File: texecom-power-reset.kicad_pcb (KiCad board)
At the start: 2 copper layers, 0 parts

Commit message: Add PCB rev A, milling footprints, fab files and project summary
- PCB rev A (92 x 70 mm, 2-layer, CNC-milled): placed and routed with the
  KiCad routing tools at 0.8 mm clearance, 15 wire-link vias, GND pours;
  DRC 0 violations / 0 unconnected, connectivity verified against schematic
- Milling footprint variants (oval enlarged pads; per-pad top keepouts on
  parts whose body covers the top pads) and custom .kicad_dru rules
- Schematic footprints assigned to the milling variants
- Gerbers (F.Cu, B.Cu, Edge.Cuts) and Excellon drill in fab/
- Copper renders and assembly drawing in docs/
- project-summary.html: one-page visual summary, linked from the README
- README: PCB section, drill table, assembly notes, decisions

Co-Authored-By: Claude Opus 5.5 <noreply@anthropic.com>
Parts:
- added C1: 100uF, texecom-power-reset:CP_Radial_D6.3mm_P2.50mm_Mill, F.Cu at (175.0, 154.0)
- added C2: 100nF, texecom-power-reset:C_Disc_D5.0mm_W2.5mm_P5.00mm_Mill, F.Cu at (166.0, 154.0)
- added C3: 10uF, texecom-power-reset:CP_Radial_D5.0mm_P2.50mm_Mill, F.Cu at (174.0, 146.0)
- added C4: 100nF, texecom-power-reset:C_Disc_D5.0mm_W2.5mm_P5.00mm_Mill, F.Cu at (132.5, 125.5)
- added C5: 10uF, Capacitor_SMD:C_1206_3216Metric_Pad1.33x1.80mm_HandSolder, B.Cu at (152.0, 113.0)
- added C6: 10uF, Capacitor_SMD:C_1206_3216Metric_Pad1.33x1.80mm_HandSolder, B.Cu at (128.5, 113.0)
- added C7: 100nF, texecom-power-reset:C_Disc_D5.0mm_W2.5mm_P5.00mm_Mill, F.Cu at (164.0, 116.0)
- added C8: 100nF, texecom-power-reset:C_Disc_D5.0mm_W2.5mm_P5.00mm_Mill, F.Cu at (116.0, 116.5)
- added D1: 1N5822, texecom-power-reset:D_DO-201AD_P15.24mm_Mill, F.Cu at (156.0, 148.0)
- added D2: P6KE18A, texecom-power-reset:D_DO-15_P10.16mm_Mill, F.Cu at (161.0, 161.0)
- added D3: 1N5822, texecom-power-reset:D_DO-201AD_P15.24mm_Mill, F.Cu at (184.0, 128.0)
- added D4: 1N4007, texecom-power-reset:D_DO-41_P10.16mm_Mill, F.Cu at (151.0, 150.5)
- added D5: 1N4007, texecom-power-reset:D_DO-41_P10.16mm_Mill, F.Cu at (125.0, 150.5)
- added D6: RED, texecom-power-reset:LED_D3.0mm_Mill, F.Cu at (148.0, 134.0)
- added D7: RED, texecom-power-reset:LED_D3.0mm_Mill, F.Cu at (122.0, 134.0)
- added F1: PTC 0.5A, Fuse:Fuse_1206_3216Metric_Pad1.42x1.75mm_HandSolder, B.Cu at (152.0, 162.0)
- added J1: BAT IN, texecom-power-reset:KF301-2P_P5.00mm_Mill, F.Cu at (142.0, 164.0)
- added J2: BAT OUT, texecom-power-reset:KF301-2P_P5.00mm_Mill, F.Cu at (130.0, 164.0)
- added J3: AC IN, texecom-power-reset:KF301-2P_P5.00mm_Mill, F.Cu at (116.0, 164.0)
- added J4: AC OUT, texecom-power-reset:KF301-2P_P5.00mm_Mill, F.Cu at (104.0, 164.0)
- added K1: SRD-05VDC, texecom-power-reset:Relay_SRD_Form_C_Mill, F.Cu at (146.6, 146.0)
- added K2: SRD-05VDC, texecom-power-reset:Relay_SRD_Form_C_Mill, F.Cu at (120.6, 146.0)
- added MH1: M3, MountingHole:MountingHole_3.2mm_M3, F.Cu at (104.0, 104.0)
- added MH2: M3, MountingHole:MountingHole_3.2mm_M3, F.Cu at (186.0, 166.0)
- added Q1: 2N2222A, texecom-power-reset:TO-92_Inline_Wide_Mill, F.Cu at (139.0, 134.0)
- added Q2: 2N2222A, texecom-power-reset:TO-92_Inline_Wide_Mill, F.Cu at (113.0, 134.0)
- added R1: 100k, texecom-power-reset:R_Axial_DIN0207_P10.16mm_Mill, F.Cu at (149.0, 108.0)
- added R10: 1k, Resistor_SMD:R_1206_3216Metric_Pad1.30x1.75mm_HandSolder, B.Cu at (165.0, 124.0)
- added R11: 100, Resistor_SMD:R_1206_3216Metric_Pad1.30x1.75mm_HandSolder, B.Cu at (152.0, 119.5)
- added R12: 100, Resistor_SMD:R_1206_3216Metric_Pad1.30x1.75mm_HandSolder, B.Cu at (128.5, 119.5)
- added R13: 10k, texecom-power-reset:R_Axial_DIN0207_P10.16mm_Mill, F.Cu at (131.5, 129.0)
- added R14: 10k, texecom-power-reset:R_Axial_DIN0207_P10.16mm_Mill, F.Cu at (105.5, 129.0)
- added R15: 1k, Resistor_SMD:R_1206_3216Metric_Pad1.30x1.75mm_HandSolder, B.Cu at (150.5, 129.0)
- added R16: 1k, Resistor_SMD:R_1206_3216Metric_Pad1.30x1.75mm_HandSolder, B.Cu at (124.5, 129.0)
- added R2: 100k, texecom-power-reset:R_Axial_DIN0207_P10.16mm_Mill, F.Cu at (111.0, 108.0)
- added R3: 1M, texecom-power-reset:R_Axial_DIN0207_P10.16mm_Mill, F.Cu at (156.0, 122.0)
- added R4: 1M, texecom-power-reset:R_Axial_DIN0207_P10.16mm_Mill, F.Cu at (124.5, 122.0)
- added R5: 10k, texecom-power-reset:R_Axial_DIN0207_P10.16mm_Mill, F.Cu at (149.0, 104.0)
- added R6: 10k, texecom-power-reset:R_Axial_DIN0207_P10.16mm_Mill, F.Cu at (111.0, 104.0)
- added R7: 1k, Resistor_SMD:R_1206_3216Metric_Pad1.30x1.75mm_HandSolder, B.Cu at (133.0, 132.5)
- added R8: 1k, Resistor_SMD:R_1206_3216Metric_Pad1.30x1.75mm_HandSolder, B.Cu at (107.0, 132.5)
- added R9: 1k, Resistor_SMD:R_1206_3216Metric_Pad1.30x1.75mm_HandSolder, B.Cu at (165.0, 108.0)
- added U1: Pololu S9V11E2F5, texecom-power-reset:Pololu_S9V11E2x_Mill, F.Cu at (161.0, 148.0)
- added U2: 74HCT4538, texecom-power-reset:DIP-16_W7.62mm_Socket_Mill, F.Cu at (144.0, 121.0)
- added U3: ESP32-C3 SuperMini, texecom-power-reset:ESP32-C3-SuperMini_Mill, F.Cu at (180.0, 111.0)
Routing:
- net +5V: track 0.00 -> 192.0 mm, vias 0 -> 2
- net Net-(U2B-R): track 0.00 -> 111.7 mm, vias 0 -> 2
- net Net-(U2B-Q): track 0.00 -> 64.8 mm
- net Net-(C5-Pad2): track 0.00 -> 54.3 mm, vias 0 -> 2
- net Net-(D4-A): track 0.00 -> 45.3 mm, vias 0 -> 1
- net Net-(U2A-R): track 0.00 -> 39.7 mm, vias 0 -> 1
- net Net-(D1-K): track 0.00 -> 37.0 mm
- net Net-(U2A-Clk+): track 0.00 -> 33.5 mm, vias 0 -> 1
- net GND: track 0.00 -> 33.5 mm, vias 0 -> 2
- net Net-(J1-Pin_1): track 0.00 -> 33.1 mm
- net Net-(U2B-Clk+): track 0.00 -> 32.7 mm
- net Net-(J3-Pin_1): track 0.00 -> 30.4 mm
- net Net-(U2A-Q): track 0.00 -> 29.4 mm, vias 0 -> 2
- net Net-(U3-IO3): track 0.00 -> 24.6 mm
- net +5V_MCU: track 0.00 -> 22.3 mm
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- added copper zone on B.Cu, net GND
- added copper zone on F.Cu, net GND
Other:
- board outline added: 92 x 70 mm

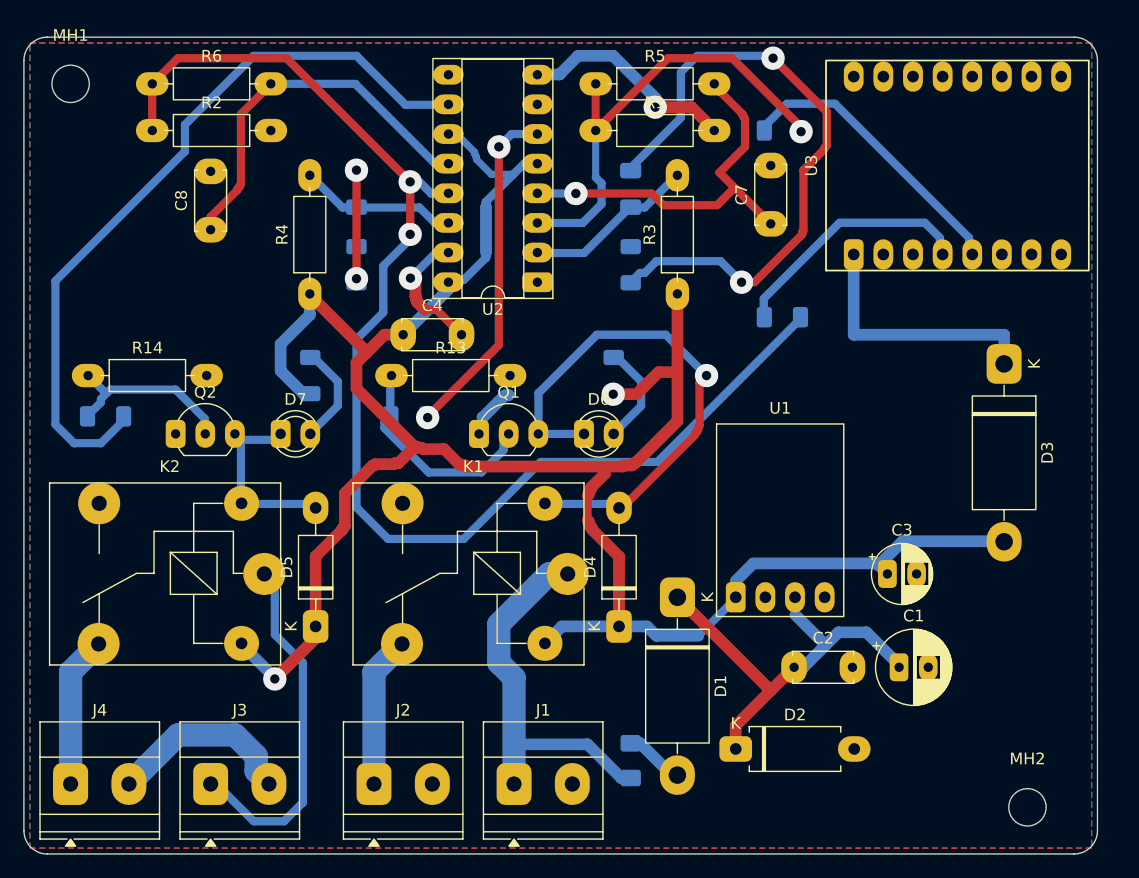
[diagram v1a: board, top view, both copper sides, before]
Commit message: Remove top GND pour and add engraved Mill_Legend layer
- GND poured on the bottom layer only; three GND pads rejoined with
  short bottom tracks and one extra via (16 vias total)
- New Mill_Legend layer (User.1): part outlines, polarity marks,
  references and BAT IN / BAT OUT / AC IN / AC OUT labels, kept 0.35mm
  clear of all top copper; exported as fab/*-Mill_Legend.gbr
- tools/make_legend.py regenerates the legend after layout changes
- Regenerated fab/ Gerbers and drill, docs/ renders
- README and project summary updated

Co-Authored-By: Claude Opus 5.5 <noreply@anthropic.com>
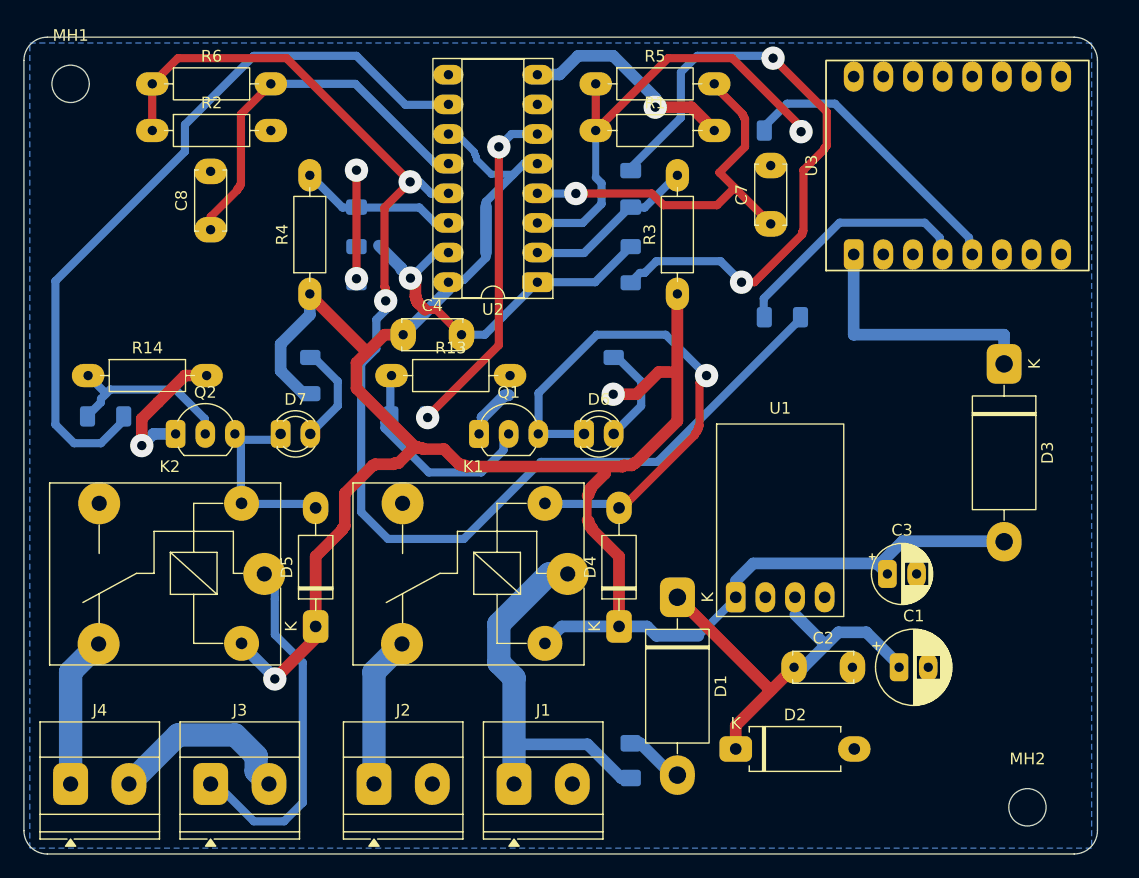
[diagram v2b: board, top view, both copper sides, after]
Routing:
- net GND: track 33.5 -> 66.8 mm, vias 2 -> 3
- removed copper zone on F.Cu, net GND
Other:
- board text added: "+"
- board text added: "-"
- board text added: "AC IN"
- board text added: "AC OUT"
- board text added: "BAT IN"
- board text added: "BAT OUT"
- board text added: "C1"
- board text added: "C2"
- board text added: "C3"
- board text added: "C4"
- board text added: "C7"
- board text added: "C8"
- board text added: "D1"
- board text added: "D2"
- board text added: "D3"
- board text added: "D4"
- board text added: "D5"
- board text added: "D6"
- board text added: "D7"
- board text added: "J1"
- board text added: "J2"
- board text added: "J3"
- board text added: "J4"
- board text added: "K1"
- board text added: "K2"
- board text added: "Q1"
- board text added: "Q2"
- board text added: "R1"
- board text added: "R13"
- board text added: "R14"
- board text added: "R2"
- board text added: "R3"
- board text added: "R4"
- board text added: "R5"
- board text added: "R6"
- board text added: "U1"
- board text added: "U2"
- board text added: "U3"

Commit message: Mark top-joint pads on the legend and add solder-top table
- Engraved ring beside each of the 20 pads that carry a top track,
  with a "o = SOLDER TOP" key; each ring is clearly nearest its pad
- README assembly step 3: table of axial/disc parts and the pads
  that must be soldered on top
- Regenerated legend Gerber, top copper SVG, assembly PDF and summary

Co-Authored-By: Claude Opus 5.5 <noreply@anthropic.com>
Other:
- board text added: "= SOLDER TOP"
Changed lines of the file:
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@@
 		(layer "User.1")
 	)
+	(gr_circle
+		(center 108.878237 105.225)
+		(end 109.378237 105.225)
+		(stroke
+			(width 0.15)
+			(type default)
+		)
+		(fill no)
+		(layer "User.1")
+	)
 	(gr_line
 		(start 109.65 145.95)
@@
 		(layer "User.1")
 	)
+	(gr_circle
+		(center 112.225 110.121762)
+		(end 112.725 110.121762)
+		(stroke
+			(width 0.15)
+			(type default)
+		)
+		(fill no)
+		(layer "User.1")
+	)
 	(gr_line
 		(start 112.55 144.15)
@@
 		(layer "User.1")
 	)
+	(gr_circle
+		(center 118.11 129)
+		(end 118.61 129)
+		(stroke
+			(width 0.15)
+			(type default)
+		)
+		(fill no)
+		(layer "User.1")
+	)
 	(gr_line
 		(start 118.114284 153.8)
@@
 		(layer "User.1")
 	)
+	(gr_circle
+		(center 118.45 116.5)
+		(end 118.95 116.5)
+		(stroke
+			(width 0.15)
+			(type default)
+		)
+		(fill no)
+		(layer "User.1")
+	)
 	(gr_line
 		(start 118.733984 105.37)
@@
 		(layer "User.1")
 	)
+	(gr_circle
+		(center 123.281762 105.225)
+		(end 123.781762 105.225)
+		(stroke
+			(width 0.15)
+			(type default)
+		)
+		(fill no)
+		(layer "User.1")
+	)
 	(gr_line
 		(start 123.36566 132.0123)
@@
 		(layer "User.1")
 	)
+	(gr_circle
+		(center 126.95 122)
+		(end 127.45 122)
+		(stroke
+			(width 0.15)
+			(type default)
+		)
+		(fill no)
+		(layer "User.1")
+	)
+	(gr_circle
+		(center 127.121762 151.725)
+		(end 127.621762 151.725)
+		(stroke
+			(width 0.15)
+			(type default)
+		)
+		(fill no)
+		(layer "User.1")
+	)
 	(gr_line
 		(start 127.38 158.68)
@@
 		(layer "User.1")
 	)
+	(gr_circle
+		(center 129.409037 124.671779)
+		(end 129.909037 124.671779)
+		(stroke
+			(width 0.15)
+			(type default)
+		)
+		(fill no)
+		(layer "User.1")
+	)
 	(gr_line
 		(start 129.699999 168.72)
@@
 		(layer "User.1")
 	)
+	(gr_circle
+		(center 138.725 123.378237)
+		(end 139.225 123.378237)
+		(stroke
+			(width 0.15)
+			(type default)
+		)
+		(fill no)
+		(layer "User.1")
+	)
 	(gr_line
 		(start 139.19 122.33)
@@
 		(layer "User.1")
 	)
+	(gr_circle
+		(center 147.775 101.878237)
+		(end 148.275 101.878237)
+		(stroke
+			(width 0.15)
+			(type default)
+		)
+		(fill no)
+		(layer "User.1")
+	)
 	(gr_line
 		(start 148 144.269707)
@@
 		(layer "User.1")
 	)
+	(gr_circle
+		(center 148.878237 151.725)
+		(end 149.378237 151.725)
+		(stroke
+			(width 0.15)
+			(type default)
+		)
+		(fill no)
+		(layer "User.1")
+	)
 	(gr_line
 		(start 148.937911 132.541165)
@@
 		(layer "User.1")
 	)
+	(gr_circle
+		(center 150.225 110.121762)
+		(end 150.725 110.121762)
+		(stroke
+			(width 0.15)
+			(type default)
+		)
+		(fill no)
+		(layer "User.1")
+	)
 	(gr_line
 		(start 150.263296 132.275626)
@@
 		(layer "User.1")
 	)
+	(gr_circle
+		(center 153.45 140.34)
+		(end 153.95 140.34)
+		(stroke
+			(width 0.15)
+			(type default)
+		)
+		(fill no)
+		(layer "User.1")
+	)
 	(gr_line
 		(start 154.63 115.155846)
@@
 		(layer "User.1")
 	)
+	(gr_circle
+		(center 156 145.25)
+		(end 156.5 145.25)
+		(stroke
+			(width 0.15)
+			(type default)
+		)
+		(fill no)
+		(layer "User.1")
+	)
 	(gr_line
 		(start 156.21576 120.19)
@@
 		(layer "User.1")
 	)
+	(gr_circle
+		(center 156.46 104)
+		(end 156.96 104)
+		(stroke
+			(width 0.15)
+			(type default)
+		)
+		(fill no)
+		(layer "User.1")
+	)
+	(gr_circle
+		(center 156.46 108)
+		(end 156.96 108)
+		(stroke
+			(width 0.15)
+			(type default)
+		)
+		(fill no)
+		(layer "User.1")
+	)
 	(gr_line
 		(start 157.35 102.63)
@@
 		(layer "User.1")
 	)
+	(gr_circle
+		(center 158.45 122)
+		(end 158.95 122)
+		(stroke
+			(width 0.15)
+			(type default)
+		)
+		(fill no)
+		(layer "User.1")
+	)
 	(gr_line
 		(start 158.72 152.175)
@@
 		(layer "User.1")
 	)
+	(gr_circle
+		(center 161 163.45)
+		(end 161.5 163.45)
+		(stroke
+			(width 0.15)
+			(type default)
+		)
+		(fill no)
+		(layer "User.1")
+	)
 	(gr_line
 		(start 162.16 162.92)
@@
 		(layer "User.1")
 	)
+	(gr_circle
+		(center 162.775 118.121762)
+		(end 163.275 118.121762)
+		(stroke
+			(width 0.15)
+			(type default)
+		)
+		(fill no)
+		(layer "User.1")
+	)
 	(gr_line
 		(start 163.10532 149.65)
@@
 		(layer "User.1")
 	)
+	(gr_circle
+		(center 166.634106 156.366518)
+		(end 167.134106 156.366518)
+		(stroke
+			(width 0.15)
+			(type default)
+		)
+		(fill no)
+		(layer "User.1")
+	)
 	(gr_line
 		(start 167.086675 152.63)
@@
 		(layer "User.1")
 	)
+	(gr_circle
+		(center 168.05 168.05)
+		(end 168.55 168.05)
+		(stroke
+			(width 0.15)
+			(type default)
+		)
+		(fill no)
+		(layer "User.1")
+	)
 	(gr_line
 		(start 168.18532 149.65)
@@
 		)
 	)
+	(gr_text "= SOLDER TOP"
+		(at 169.15 168.05 0)
+		(layer "User.1")
+		(effects
+			(font
+				(size 1.2 1.2)
+				(thickness 0.15)
+			)
+			(justify left)
+		)
+	)

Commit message: Correct mirrored SuperMini footprint; rotate U3, swap GPIO3/GPIO4
- ESP32-C3-SuperMini footprints: pin rows were mirrored (matched the
  bottom-view pinout drawing); corrected so the module mounts button
  side up
- U3 rotated 180 deg: USB-C at the board edge, original routing kept
  (DRC 0/0, 16 vias); antenna keepout removed
- Schematic: GPIO4 -> channel 1 (K1 battery), GPIO3 -> channel 2 (K2 AC)
- Legend: "USB ->" arrow on U3
- BOM: optional Communica IPEX WiFi antenna
- README (Tasmota GPIO table, V2 WS2812 on GPIO8, orientation,
  decisions), regenerated fab/, docs/, schematic PDF and summary

Co-Authored-By: Claude Opus 5.5 <noreply@anthropic.com>
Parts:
- turned U3 to -90 degrees
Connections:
- R10 pad 1: Net-(U3-IO4) -> Net-(U3-IO3)
- R9 pad 1: Net-(U3-IO3) -> Net-(U3-IO4)
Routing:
- net +5V_MCU: track 22.3 -> 11.4 mm
- net Net-(U3-IO4): track 21.2 -> 24.6 mm
- net Net-(U3-IO3): track 24.6 -> 21.2 mm
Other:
- board text added: "USB"
